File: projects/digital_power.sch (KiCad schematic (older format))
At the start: 6 parts, among them U501 LT1763

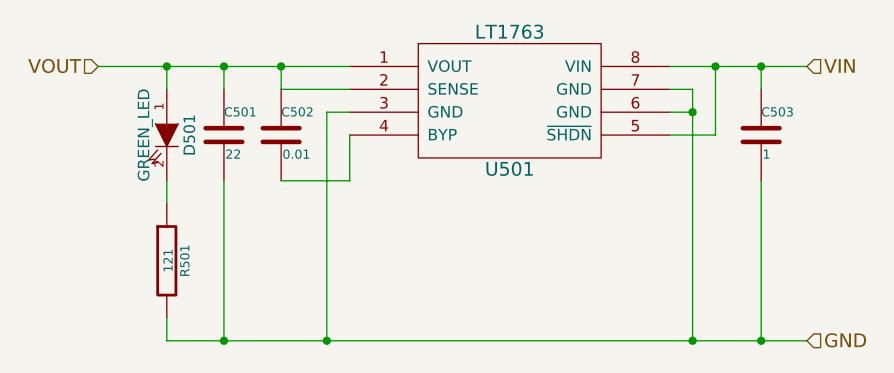
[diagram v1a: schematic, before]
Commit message: add box cap and small electrolytic cap footprints
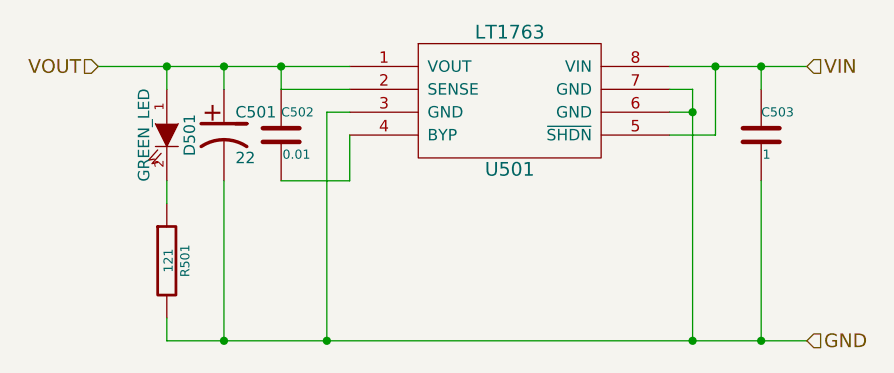
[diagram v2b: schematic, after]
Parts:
- removed C501: 22, symbol C
- added C501: 22, symbol CP1
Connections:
- net GND: now also C501.2
- net VOUT: now also C501.1
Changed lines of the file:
@@
-	1    0    0    -1
-$EndComp
-$Comp
-L C C501
-U 1 1 54571D8D
-P 4450 4150
-F 0 "C501" H 4450 4250 40  0000 L CNN
-F 1 "22" H 4456 4065 40  0000 L CNN
-F 2 "" H 4488 4000 30  0000 C CNN
-F 3 "" H 4450 4150 60  0000 C CNN
-F 4 "Digi-Key" H 4450 4150 60  0001 C CNN "Supplier"
-F 5 "P16405CT-ND" H 4450 4150 60  0001 C CNN "Supplier-PN"
-F 6 "Panasonic" H 4450 4150 60  0001 C CNN "Manu"
-F 7 "32SEPF22M+TSS" H 4450 4150 60  0001 C CNN "Manu-PN"
-F 8 "CAP ALUM 22UF 32V 20% RADIAL" H 4450 4150 60  0001 C CNN "Description"
-	1    4450 4150
 	1    0    0    -1
 $EndComp
@@
 	4200 5050 4200 4950
 Connection ~ 4450 5050
+$Comp
+L CP1 C501
+U 1 1 5485939A
+P 4450 4150
+F 0 "C501" H 4500 4250 50  0000 L CNN
+F 1 "22" H 4500 4050 50  0000 L CNN
+F 2 "" H 4450 4150 60  0000 C CNN
+F 3 "" H 4450 4150 60  0000 C CNN
+F 4 "Digi-key" H 4450 4150 60  0001 C CNN "Supplier"
+F 5 "P16405CT-ND" H 4450 4150 60  0001 C CNN "Supplier-PN"
+F 6 "Panasonic" H 4450 4150 60  0001 C CNN "Manu"
+F 7 "32SEPF22M+TSS" H 4450 4150 60  0001 C CNN "Manu-PN"
+F 8 "CAP ALUM 22UF 32V 20% RADIAL" H 4450 4150 60  0001 C CNN "Description"
+	1    4450 4150
+	1    0    0    -1
+$EndComp
 $EndSCHEMATC
